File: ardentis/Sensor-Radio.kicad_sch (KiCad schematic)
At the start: 15 parts, among them IC1 ICM-42670-P, IC2 317990687, IC4 L86-M33, J3 Conn_Coaxial_Small, U2 LPS22HH

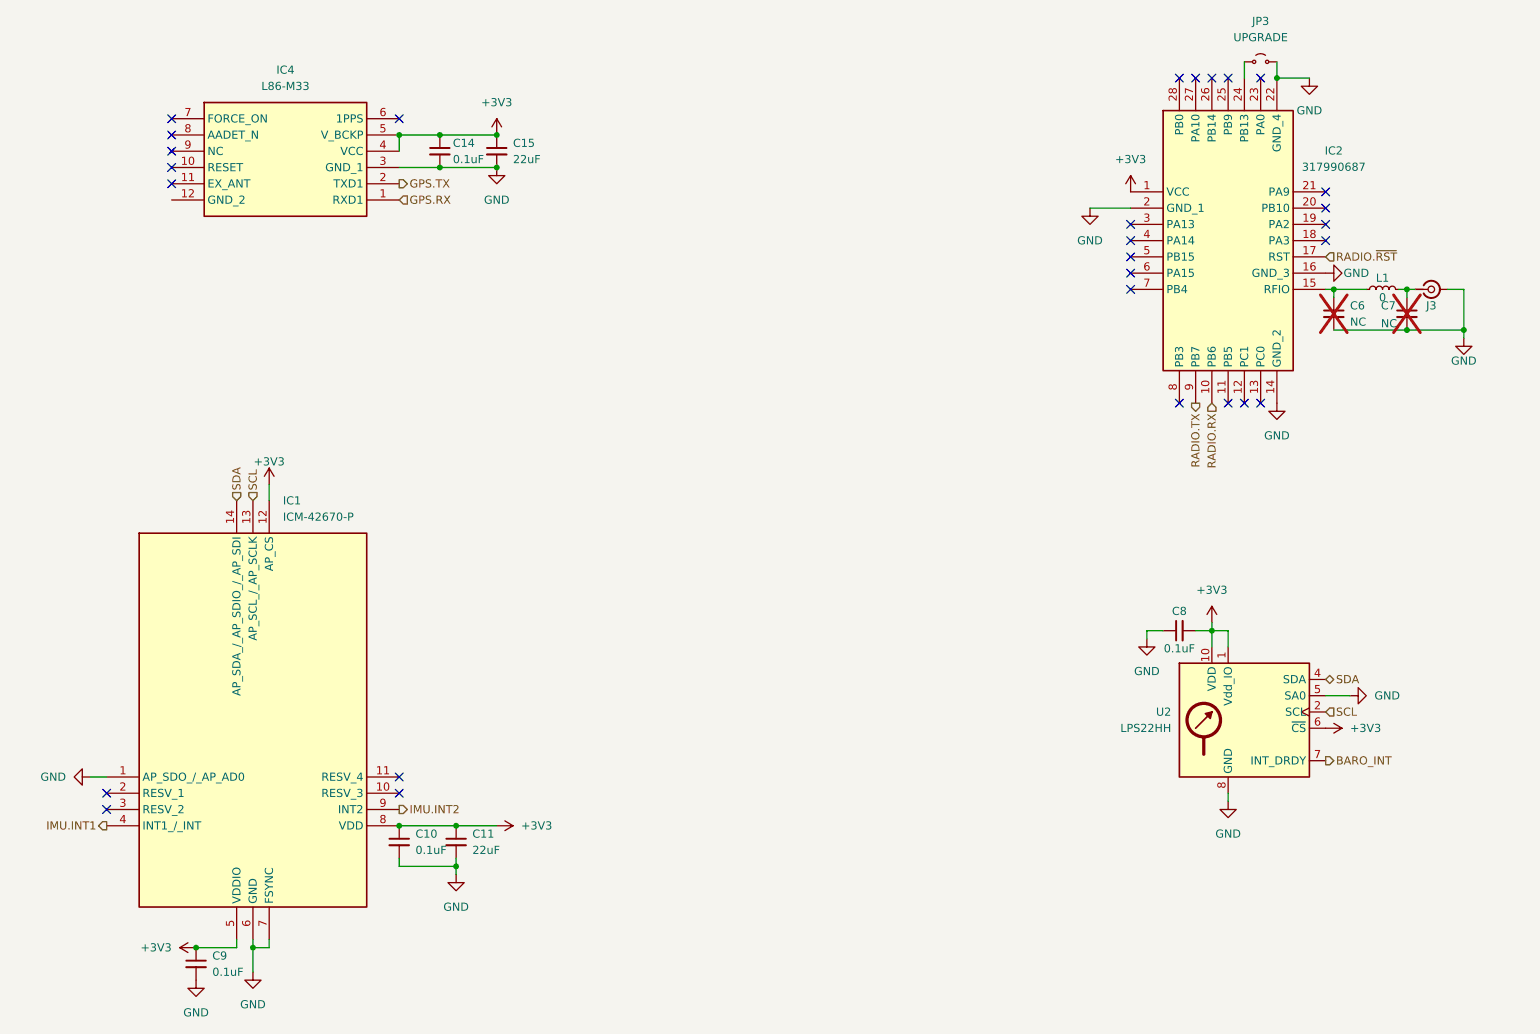
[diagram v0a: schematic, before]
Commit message: Initial code
Initial code. Theoretically will work but not tested due to lack of hardware and updates to PCB.
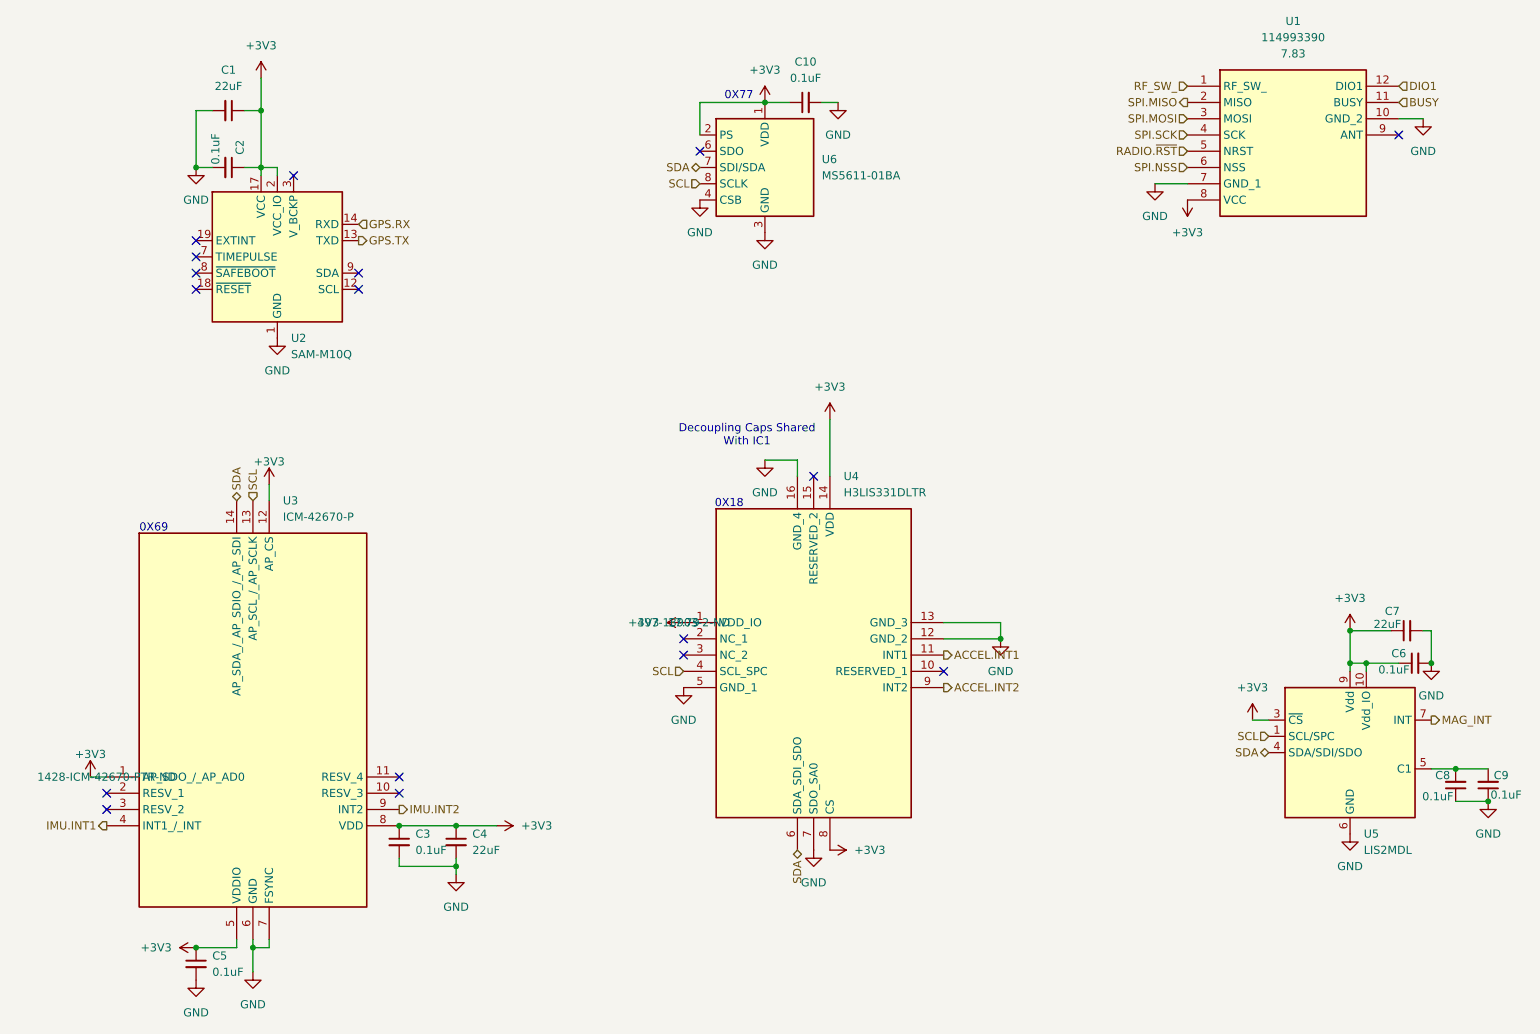
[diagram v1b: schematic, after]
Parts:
- removed C6, C7: NC, symbol Device:C_Small
- removed C8: 0.1uF, symbol Device:C_Small
- removed IC2: 317990687, 317990687, symbol 317990687:317990687
- removed IC4: L86-M33, L80-M39, symbol L86-M33:L86-M33
- removed J3: Conn_Coaxial_Small, symbol Connector:Conn_Coaxial_Small
- removed JP3: UPGRADE, symbol Jumper:Jumper_2_Small_Open
- removed L1: 0, symbol Device:L_Small
- removed U2: LPS22HH, Package_LGA:ST_HLGA-10_2x2mm_P0.5mm_LayoutBorder3x2y, symbol Sensor_Pressure:LPS22HH
- added C10, C6, C8, C9: 0.1uF, Library:C_0805_2012Metric_Pad1.18x1.45mm_HandSolder, symbol Library:C_Small
- added C7: 22uF, Library:C_0805_2012Metric_Pad1.18x1.45mm_HandSolder, symbol Library:C_Small
- added U1: 114993390, Library:114993390, symbol Library:114993390
- added U2: SAM-M10Q, Library:ublox_SAM-M10Q, symbol Library:SAM-M10Q
- added U4: H3LIS331DLTR, Library:H3LIS331DLTR, symbol Library:H3LIS331DLTR
- added U5: LIS2MDL, Library:LGA-12_2x2mm_P0.5mm, symbol Library:LIS2MDL
- added U6: MS5611-01BA, Library:LGA-8_3x5mm_P1.25mm, symbol Library:MS5611-01BA
- C1: renamed from C15; footprint (none) -> Library:C_0805_2012Metric_Pad1.18x1.45mm_HandSolder; symbol Device:C_Small -> Library:C_Small; Manufacturer_Name Murata Electronics -> Samsung Electro-Mechanics; Manufacturer_Part_Number GRM21BZ70J226ME44L -> CL21X226MQQNNNE; Price 0.293 -> 0.2; SPN (none) -> 1276-3031-2-ND; Var (none) -> Variant Ground(-!) Flight(+!)
- C2: renamed from C14; footprint (none) -> Library:C_0805_2012Metric_Pad1.18x1.45mm_HandSolder; symbol Device:C_Small -> Library:C_Small; Manufacturer_Part_Number 08053C104KAT2A -> KGM21NR71H104KT; Price 0.07 -> 0.12; SPN (none) -> 478-KGM21NR71H104KTTR-ND; Var (none) -> Variant Ground(-!) Flight(+!)
- C3: renamed from C10; footprint (none) -> Library:C_0805_2012Metric_Pad1.18x1.45mm_HandSolder; symbol Device:C_Small -> Library:C_Small; Manufacturer_Part_Number 08053C104KAT2A -> KGM21NR71H104KT; Price 0.07 -> 0.12; SPN (none) -> 478-KGM21NR71H104KTTR-ND; Var (none) -> Variant Ground(-!) Flight(+!)
- C4: renamed from C11; footprint (none) -> Library:C_0805_2012Metric_Pad1.18x1.45mm_HandSolder; symbol Device:C_Small -> Library:C_Small; Manufacturer_Name Murata Electronics -> Samsung Electro-Mechanics; Manufacturer_Part_Number GRM21BZ70J226ME44L -> CL21X226MQQNNNE; Price 0.293 -> 0.2; SPN (none) -> 1276-3031-2-ND; Var (none) -> Variant Ground(-!) Flight(+!)
- C5: renamed from C9; footprint (none) -> Library:C_0805_2012Metric_Pad1.18x1.45mm_HandSolder; symbol Device:C_Small -> Library:C_Small; Manufacturer_Part_Number 08053C104KAT2A -> KGM21NR71H104KT; Price 0.07 -> 0.12; SPN (none) -> 478-KGM21NR71H104KTTR-ND; Var (none) -> Variant Ground(-!) Flight(+!)
- U3: renamed from IC1; footprint ICM42670P -> Library:ICM42670P; symbol ICM-42670-P:ICM-42670-P -> Library:ICM-42670-P; Price 5.31 -> 5.90; SPN (none) -> 1428-ICM-42670-PTR-ND; Var (none) -> Variant Ground(-!) Flight(+!)
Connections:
- net +3V3: now also U3.1 (AP_SDO_/_AP_AD0), C10.1, C6.1, C7.1, U1.8 (VCC), U2.17 (VCC), U2.2 (VCC_IO), U4.1 (VDD_IO), U4.14 (VDD), U4.8 (CS), U5.10 (Vdd_IO), U5.3 (~{CS}), U5.9 (Vdd), U6.1 (VDD), U6.2 (PS)
- net GND: now also C10.2, C6.2, C7.2, C8.1, C9.1, U1.10 (GND_2), U1.7 (GND_1), U2.1 (GND), U2.10 (GND), U2.11 (GND), U2.15 (GND), U2.16 (GND), U2.20 (GND), U2.4 (GND), U2.5 (GND), U2.6 (GND), U4.12 (GND_2), U4.13 (GND_3), U4.16 (GND_4), U4.5 (GND_1), U4.7 (SDO_SA0), U5.6 (GND), U5.8 (GND), U6.3 (GND), U6.4 (CSB), U6.5 (CSB); no longer U3.1 (AP_SDO_/_AP_AD0)
- net GPS.RX: now also U2.14 (RXD)
- net GPS.TX: now also U2.13 (TXD)
- net RADIO.~{RST}: now also U1.5 (NRST)
- net SCL: now also U4.4 (SCL_SPC), U5.1 (SCL/SPC), U6.8 (SCLK)
- net SDA: now also U4.6 (SDA_SDI_SDO), U5.4 (SDA/SDI/SDO), U6.7 (SDI/SDA)
- new net: C8.2, C9.2, U5.5 (C1)
- new net ACCEL.INT1: U4.11 (INT1)
- new net ACCEL.INT2: U4.9 (INT2)
- new net BUSY: U1.11 (BUSY)
- new net DIO1: U1.12 (DIO1)
- new net MAG_INT: U5.7 (DRDY)
- new net RF_SW_: U1.1 (RF_SW_)
- new net SPI.MISO: U1.2 (MISO)
- new net SPI.MOSI: U1.3 (MOSI)
- new net SPI.NSS: U1.6 (NSS)
- new net SPI.SCK: U1.4 (SCK)
- no-connect marks 28 -> 17
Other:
- note added: "0X18"
- note added: "0X69"
- note added: "0X77"
- note added: "Decoupling Caps Shared With IC1"
- company: (none) -> CU INSPACE
- moved on the sheet: C1, C2
